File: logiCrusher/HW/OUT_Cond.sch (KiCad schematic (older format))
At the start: 21 parts

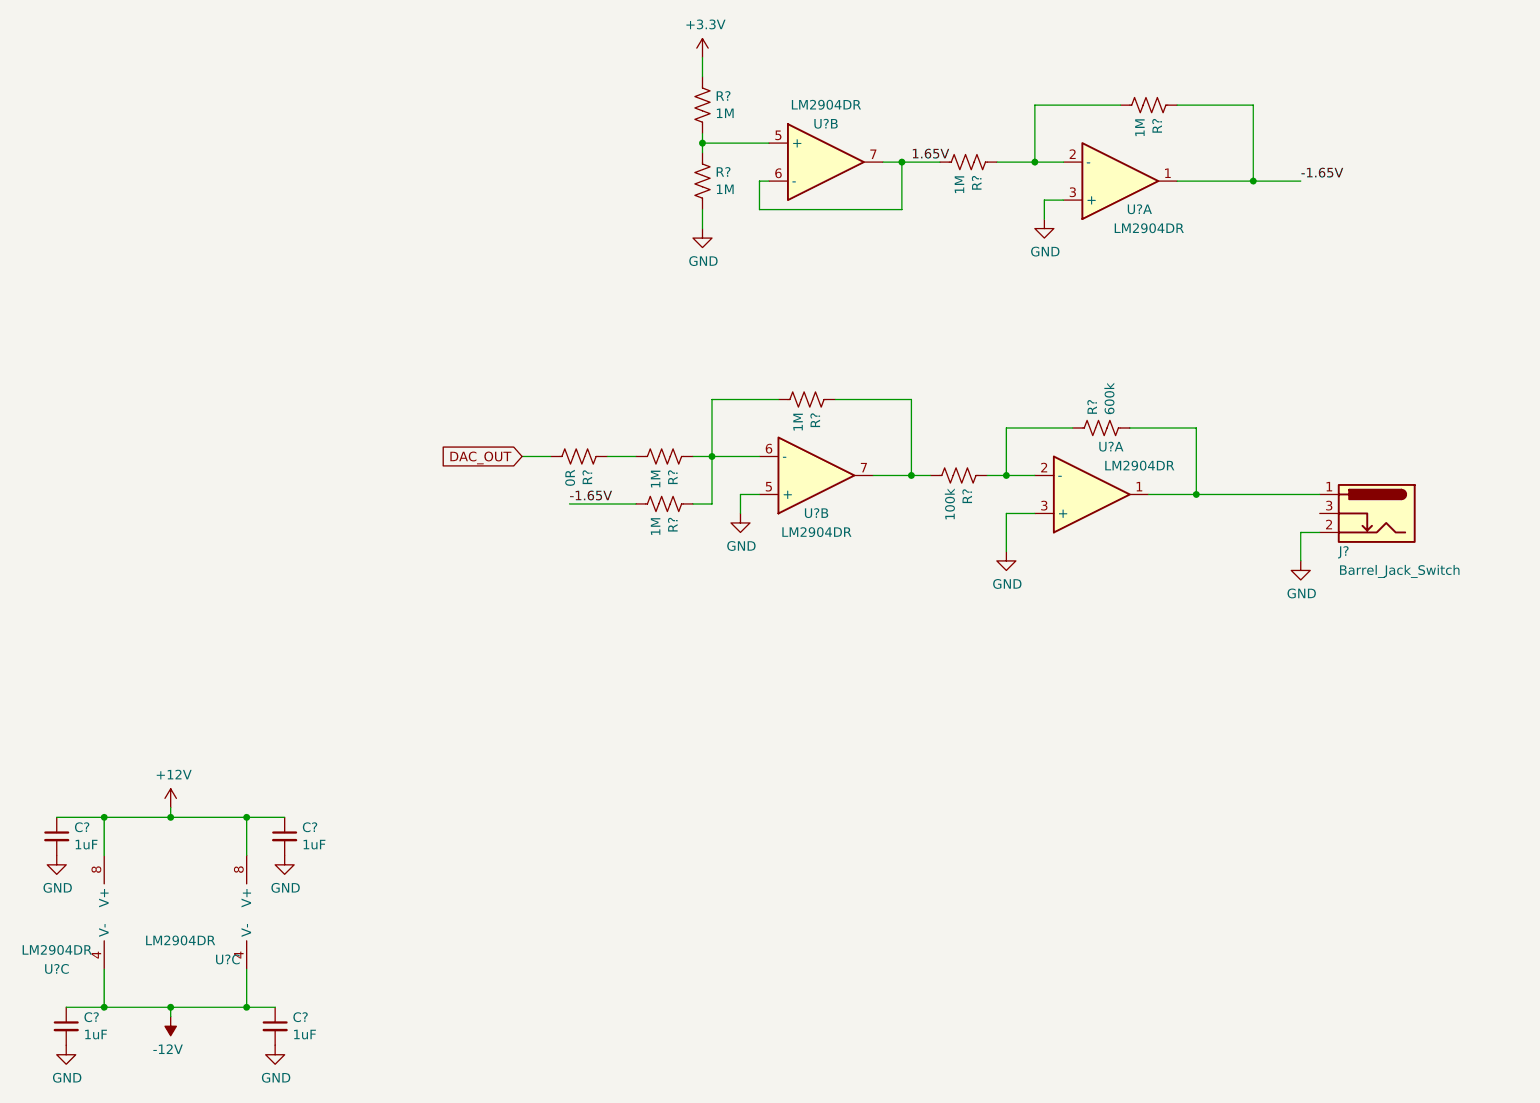
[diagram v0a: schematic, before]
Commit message: Added the front plate files
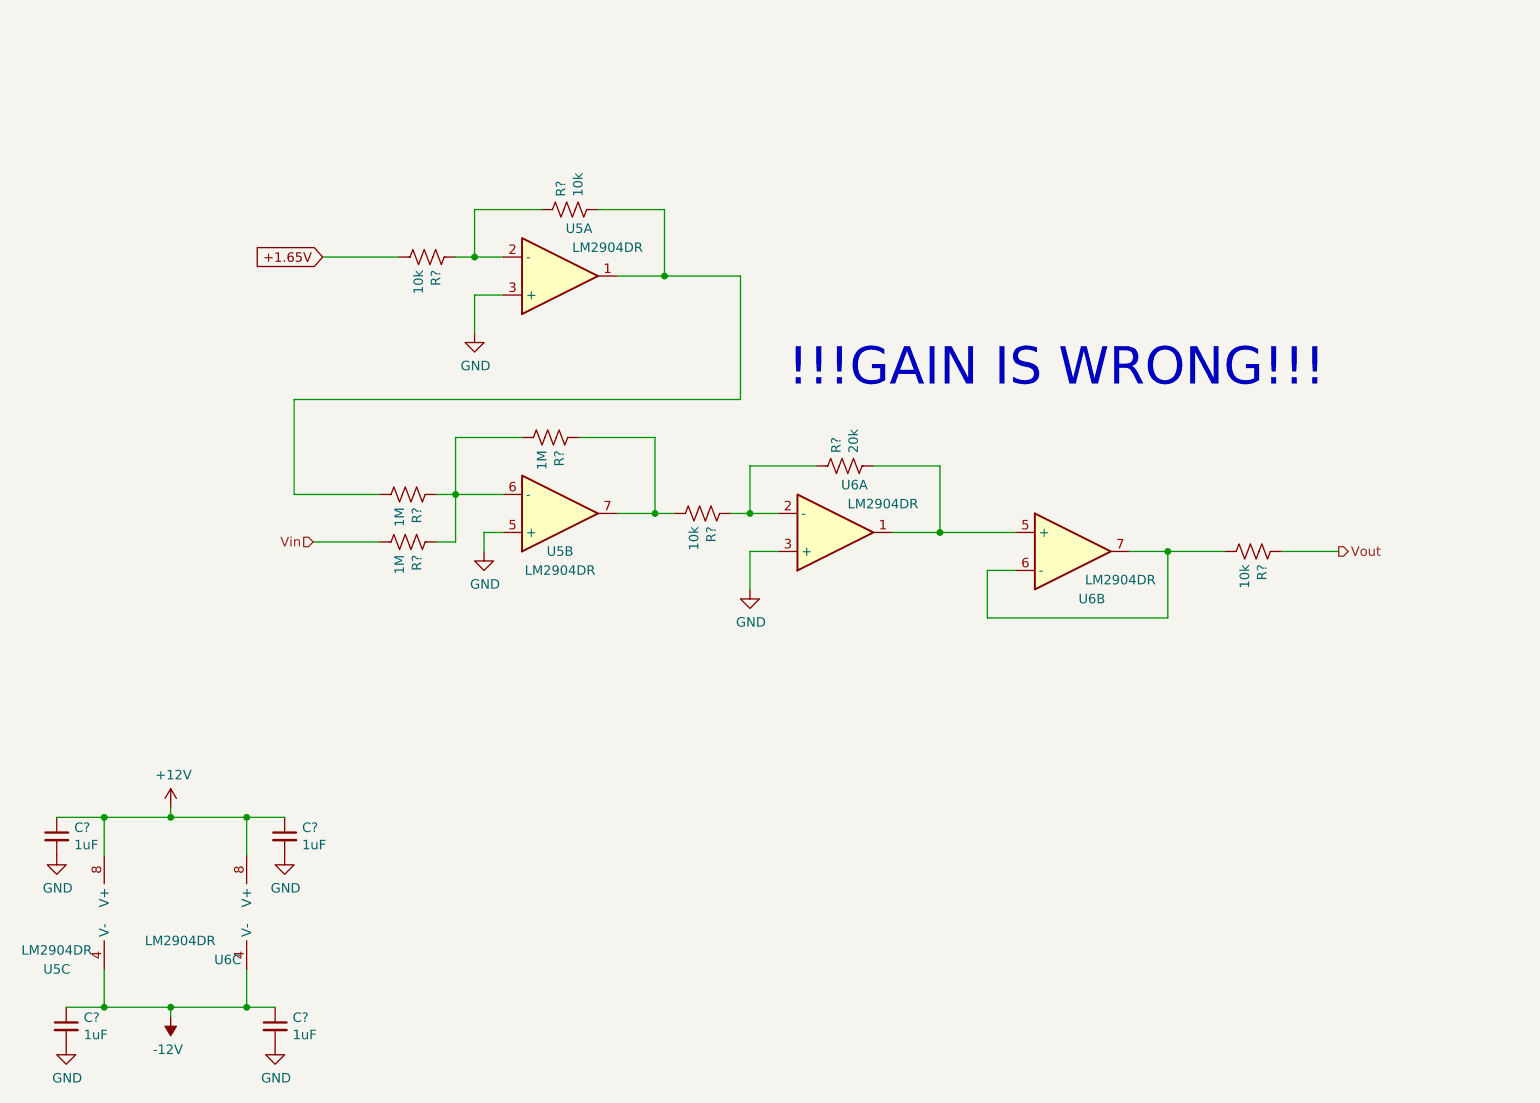
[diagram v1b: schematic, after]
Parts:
- removed J?: Barrel_Jack_Switch, Eurocad:PJ301M-12, symbol Connector:Barrel_Jack_Switch
- removed R?: 0R, Resistor_SMD:R_0805_2012Metric, symbol Device:R_US
- removed R? (x4): 1M, Resistor_SMD:R_0805_2012Metric, symbol Device:R_US
- removed U? (x2): LM2904DR, Package_SO:SOIC-8_3.9x4.9mm_P1.27mm, symbol Device:Opamp_Dual_Generic
- added R? (x3): 10k, Resistor_SMD:R_0805_2012Metric, symbol Device:R_US
- added unit 1 of U5
- added unit 2 of U6
- R?: value 600k -> 20k
- R?: value 100k -> 10k
- gave numbers to parts that had none: 2
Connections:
- net GND: now also U5.3 (+)
- net at R?.1: now also R?.1, U5.1
- net at R?.1, U6.1: now also U6.5 (+)
- net -1.65V renamed Vin
- new net: R?.1, U6.6 (-), U6.7
- new net: R?.2, R?.2, U5.2 (-)
- new net +1.65V: R?.1
- new net Vout: R?.2
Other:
- note added: "!!!GAIN IS WRONG!!!"
- moved on the sheet: R?, U5B, U6A

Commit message: Worked on the HW for the mcu module
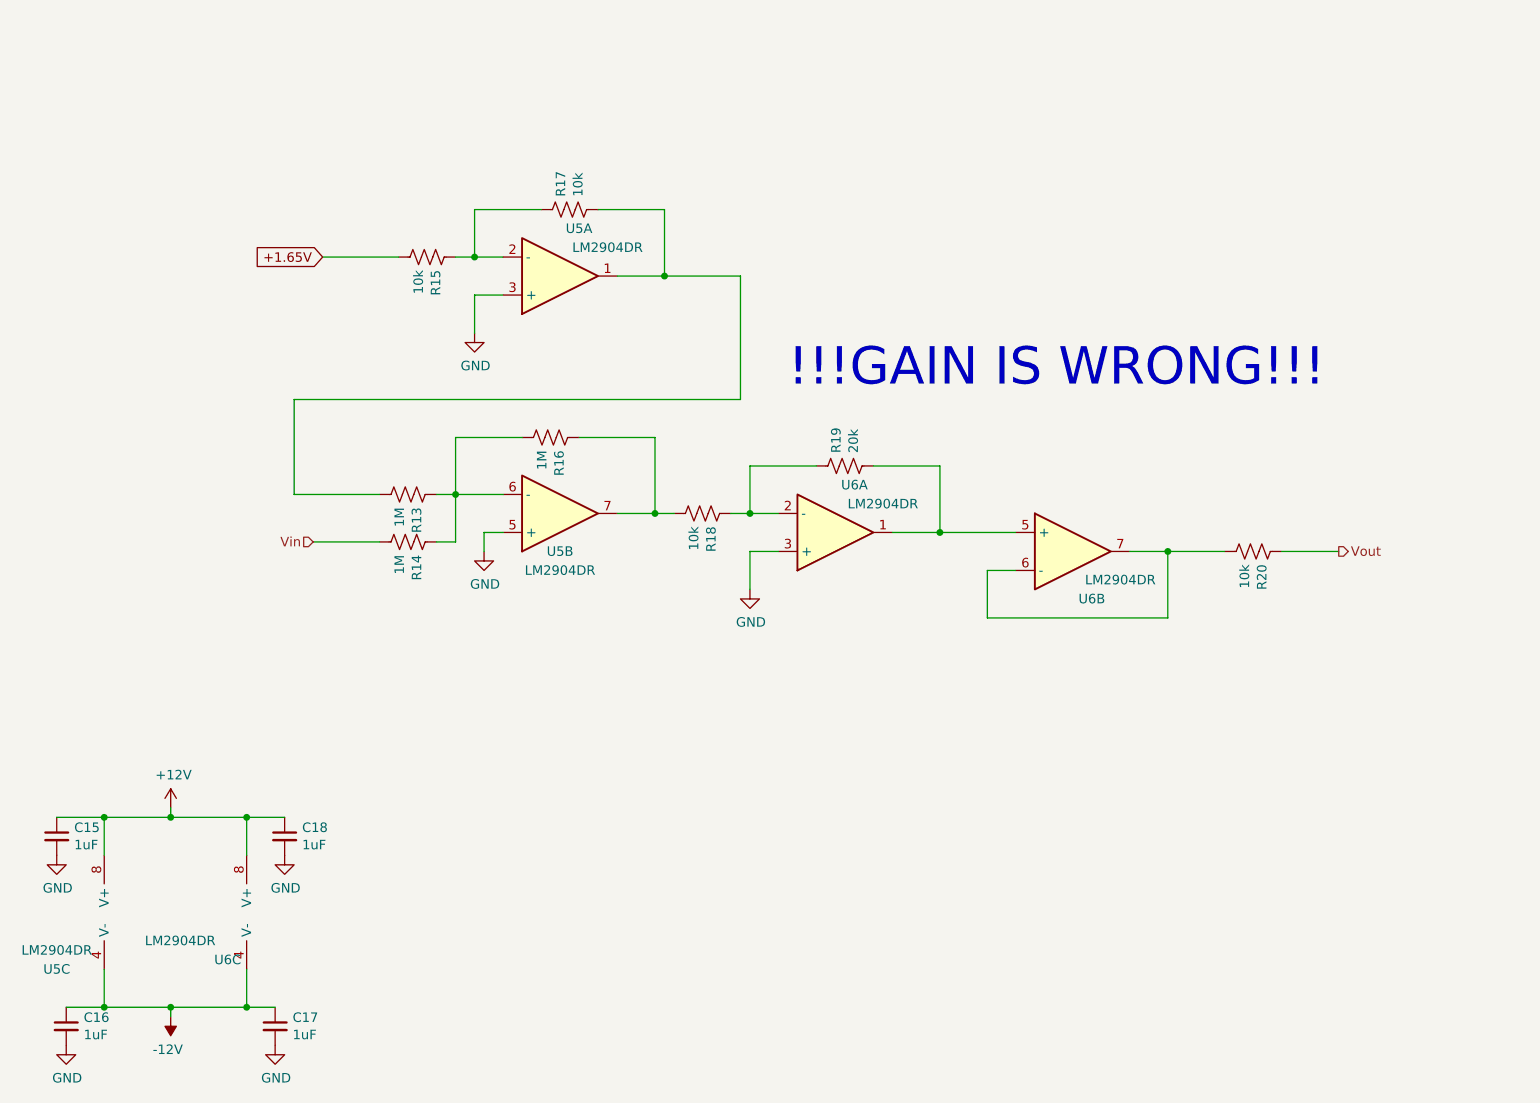
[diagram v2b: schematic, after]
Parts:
- gave numbers to parts that had none: 12
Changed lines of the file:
@@
 P 4750 4900
 AR Path="/5CBB18CB" Ref="#PWR?"  Part="1"
-AR Path="/5CBAEA8D/5CBB18CB" Ref="#PWR?"  Part="1"
-F 0 "#PWR?" H 4750 4650 50  0001 C CNN
+AR Path="/5CBAEA8D/5CBB18CB" Ref="#PWR053"  Part="1"
+F 0 "#PWR053" H 4750 4650 50  0001 C CNN
 F 1 "GND" H 4755 4727 50  0000 C CNN
 F 2 "" H 4750 4900 50  0001 C CNN
@@
 P 5250 4250
 AR Path="/5CBB18D3" Ref="R?"  Part="1"
-AR Path="/5CBAEA8D/5CBB18D3" Ref="R?"  Part="1"
-F 0 "R?" H 5182 4204 50  0000 R CNN
+AR Path="/5CBAEA8D/5CBB18D3" Ref="R19"  Part="1"
+F 0 "R19" H 5182 4204 50  0000 R CNN
 F 1 "20k" H 5182 4295 50  0000 R CNN
 F 2 "Resistor_SMD:R_0805_2012Metric" V 5290 4240 50  0001 C CNN
@@
 P 4500 4500
 AR Path="/5CBB18DA" Ref="R?"  Part="1"
-AR Path="/5CBAEA8D/5CBB18DA" Ref="R?"  Part="1"
-F 0 "R?" H 4432 4454 50  0000 R CNN
+AR Path="/5CBAEA8D/5CBB18DA" Ref="R18"  Part="1"
+F 0 "R18" H 4432 4454 50  0000 R CNN
 F 1 "10k" H 4432 4545 50  0000 R CNN
 F 2 "Resistor_SMD:R_0805_2012Metric" V 4540 4490 50  0001 C CNN
@@
 P 3700 4100
 AR Path="/5CBB18F1" Ref="R?"  Part="1"
-AR Path="/5CBAEA8D/5CBB18F1" Ref="R?"  Part="1"
-F 0 "R?" H 3632 4054 50  0000 R CNN
+AR Path="/5CBAEA8D/5CBB18F1" Ref="R16"  Part="1"
+F 0 "R16" H 3632 4054 50  0000 R CNN
 F 1 "1M" H 3632 4145 50  0000 R CNN
 F 2 "Resistor_SMD:R_0805_2012Metric" V 3740 4090 50  0001 C CNN
@@
 P 3350 4700
 AR Path="/5CBB1900" Ref="#PWR?"  Part="1"
-AR Path="/5CBAEA8D/5CBB1900" Ref="#PWR?"  Part="1"
-F 0 "#PWR?" H 3350 4450 50  0001 C CNN
+AR Path="/5CBAEA8D/5CBB1900" Ref="#PWR052"  Part="1"
+F 0 "#PWR052" H 3350 4450 50  0001 C CNN
 F 1 "GND" H 3355 4527 50  0000 C CNN
 F 2 "" H 3350 4700 50  0001 C CNN
@@
 P 2950 4650
 AR Path="/5CBB1908" Ref="R?"  Part="1"
-AR Path="/5CBAEA8D/5CBB1908" Ref="R?"  Part="1"
-F 0 "R?" H 2882 4604 50  0000 R CNN
+AR Path="/5CBAEA8D/5CBB1908" Ref="R14"  Part="1"
+F 0 "R14" H 2882 4604 50  0000 R CNN
 F 1 "1M" H 2882 4695 50  0000 R CNN
 F 2 "Resistor_SMD:R_0805_2012Metric" V 2990 4640 50  0001 C CNN
@@
 P 2950 4400
 AR Path="/5CBB190F" Ref="R?"  Part="1"
-AR Path="/5CBAEA8D/5CBB190F" Ref="R?"  Part="1"
-F 0 "R?" H 2882 4354 50  0000 R CNN
+AR Path="/5CBAEA8D/5CBB190F" Ref="R13"  Part="1"
+F 0 "R13" H 2882 4354 50  0000 R CNN
 F 1 "1M" H 2882 4445 50  0000 R CNN
 F 2 "Resistor_SMD:R_0805_2012Metric" V 2990 4390 50  0001 C CNN
@@
 $EndComp
 $Comp
-L power:+12V #PWR?
+L power:+12V #PWR047
 U 1 1 5CBB493F
 P 1700 6050
-F 0 "#PWR?" H 1700 5900 50  0001 C CNN
+F 0 "#PWR047" H 1700 5900 50  0001 C CNN
 F 1 "+12V" H 1715 6223 50  0000 C CNN
 F 2 "" H 1700 6050 50  0001 C CNN
@@
 $EndComp
 $Comp
-L power:-12V #PWR?
+L power:-12V #PWR048
 U 1 1 5CBB4945
 P 1700 7150
-F 0 "#PWR?" H 1700 7250 50  0001 C CNN
+F 0 "#PWR048" H 1700 7250 50  0001 C CNN
 F 1 "-12V" H 1715 7323 50  0000 C CNN
 F 2 "" H 1700 7150 50  0001 C CNN
@@
 	1700 7150 1700 7100
 $Comp
-L Device:C_Small C?
+L Device:C_Small C17
 U 1 1 5CBB4957
 P 2250 7200
-F 0 "C?" H 2342 7246 50  0000 L CNN
+F 0 "C17" H 2342 7246 50  0000 L CNN
 F 1 "1uF" H 2342 7155 50  0000 L CNN
 F 2 "Capacitor_SMD:C_0805_2012Metric" H 2250 7200 50  0001 C CNN
@@
 $EndComp
 $Comp
-L Device:C_Small C?
+L Device:C_Small C16
 U 1 1 5CBB495E
 P 1150 7200
-F 0 "C?" H 1242 7246 50  0000 L CNN
+F 0 "C16" H 1242 7246 50  0000 L CNN
 F 1 "1uF" H 1242 7155 50  0000 L CNN
 F 2 "Capacitor_SMD:C_0805_2012Metric" H 1150 7200 50  0001 C CNN
@@
 $EndComp
 $Comp
-L Device:C_Small C?
+L Device:C_Small C18
 U 1 1 5CBB4965
 P 2300 6200
-F 0 "C?" H 2392 6246 50  0000 L CNN
+F 0 "C18" H 2392 6246 50  0000 L CNN
 F 1 "1uF" H 2392 6155 50  0000 L CNN
 F 2 "Capacitor_SMD:C_0805_2012Metric" H 2300 6200 50  0001 C CNN
@@
 $EndComp
 $Comp
-L Device:C_Small C?
+L Device:C_Small C15
 U 1 1 5CBB496C
 P 1100 6200
-F 0 "C?" H 1192 6246 50  0000 L CNN
+F 0 "C15" H 1192 6246 50  0000 L CNN
 F 1 "1uF" H 1192 6155 50  0000 L CNN
 F 2 "Capacitor_SMD:C_0805_2012Metric" H 1100 6200 50  0001 C CNN
@@
 Connection ~ 1350 7100
 $Comp
-L power:GND #PWR?
+L power:GND #PWR045
 U 1 1 5CBB497B
 P 1100 6300
-F 0 "#PWR?" H 1100 6050 50  0001 C CNN
+F 0 "#PWR045" H 1100 6050 50  0001 C CNN
 F 1 "GND" H 1105 6127 50  0000 C CNN
 F 2 "" H 1100 6300 50  0001 C CNN
@@
 $EndComp
 $Comp
-L power:GND #PWR?
+L power:GND #PWR050
 U 1 1 5CBB4981
 P 2300 6300
-F 0 "#PWR?" H 2300 6050 50  0001 C CNN
+F 0 "#PWR050" H 2300 6050 50  0001 C CNN
 F 1 "GND" H 2305 6127 50  0000 C CNN
 F 2 "" H 2300 6300 50  0001 C CNN
@@
 $EndComp
 $Comp
-L power:GND #PWR?
+L power:GND #PWR049
 U 1 1 5CBB4987
 P 2250 7300
-F 0 "#PWR?" H 2250 7050 50  0001 C CNN
+F 0 "#PWR049" H 2250 7050 50  0001 C CNN
 F 1 "GND" H 2255 7127 50  0000 C CNN
 F 2 "" H 2250 7300 50  0001 C CNN
@@
 $EndComp
 $Comp
-L power:GND #PWR?
+L power:GND #PWR046
 U 1 1 5CBB498D
 P 1150 7300
-F 0 "#PWR?" H 1150 7050 50  0001 C CNN
+F 0 "#PWR046" H 1150 7050 50  0001 C CNN
 F 1 "GND" H 1155 7127 50  0000 C CNN
 F 2 "" H 1150 7300 50  0001 C CNN
@@
 P 7400 4700
 AR Path="/5CB6A68A" Ref="R?"  Part="1"
-AR Path="/5CBAEA8D/5CB6A68A" Ref="R?"  Part="1"
-F 0 "R?" H 7332 4654 50  0000 R CNN
+AR Path="/5CBAEA8D/5CB6A68A" Ref="R20"  Part="1"
+F 0 "R20" H 7332 4654 50  0000 R CNN
 F 1 "10k" H 7332 4745 50  0000 R CNN
 F 2 "Resistor_SMD:R_0805_2012Metric" V 7440 4690 50  0001 C CNN
@@
 P 3300 3550
 AR Path="/5CB6AC35" Ref="#PWR?"  Part="1"
-AR Path="/5CBAEA8D/5CB6AC35" Ref="#PWR?"  Part="1"
-F 0 "#PWR?" H 3300 3300 50  0001 C CNN
+AR Path="/5CBAEA8D/5CB6AC35" Ref="#PWR051"  Part="1"
+F 0 "#PWR051" H 3300 3300 50  0001 C CNN
 F 1 "GND" H 3305 3377 50  0000 C CNN
 F 2 "" H 3300 3550 50  0001 C CNN
@@
 P 3800 2900
 AR Path="/5CB6AC3D" Ref="R?"  Part="1"
-AR Path="/5CBAEA8D/5CB6AC3D" Ref="R?"  Part="1"
-F 0 "R?" H 3732 2854 50  0000 R CNN
+AR Path="/5CBAEA8D/5CB6AC3D" Ref="R17"  Part="1"
+F 0 "R17" H 3732 2854 50  0000 R CNN
 F 1 "10k" H 3732 2945 50  0000 R CNN
 F 2 "Resistor_SMD:R_0805_2012Metric" V 3840 2890 50  0001 C CNN
@@
 P 3050 3150
 AR Path="/5CB6AC44" Ref="R?"  Part="1"
-AR Path="/5CBAEA8D/5CB6AC44" Ref="R?"  Part="1"
-F 0 "R?" H 2982 3104 50  0000 R CNN
+AR Path="/5CBAEA8D/5CB6AC44" Ref="R15"  Part="1"
+F 0 "R15" H 2982 3104 50  0000 R CNN
 F 1 "10k" H 2982 3195 50  0000 R CNN
 F 2 "Resistor_SMD:R_0805_2012Metric" V 3090 3140 50  0001 C CNN

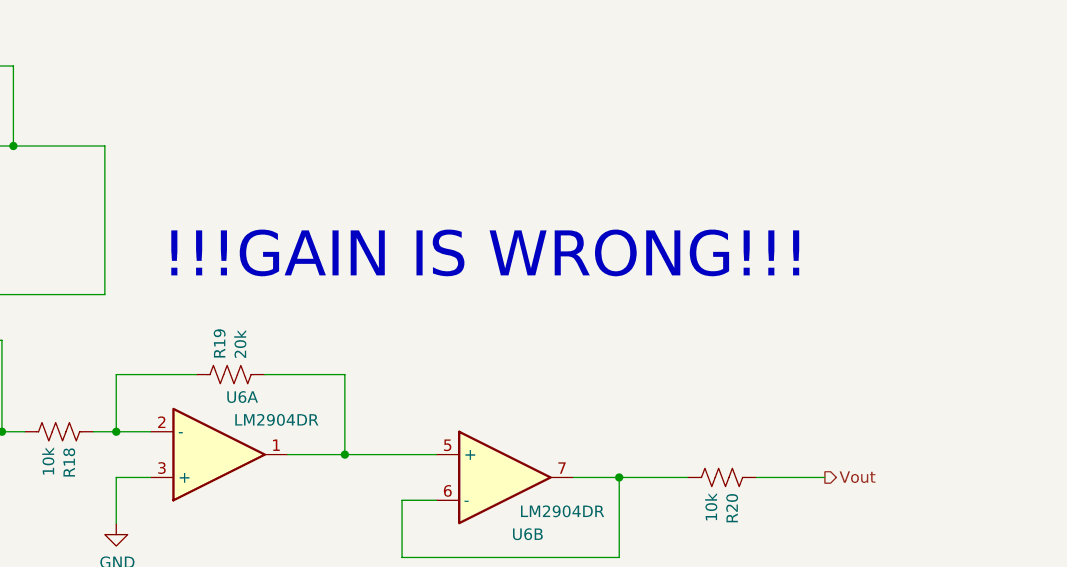
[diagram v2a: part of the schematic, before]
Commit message: Added simulation files and fixed the values of the gain resistors.
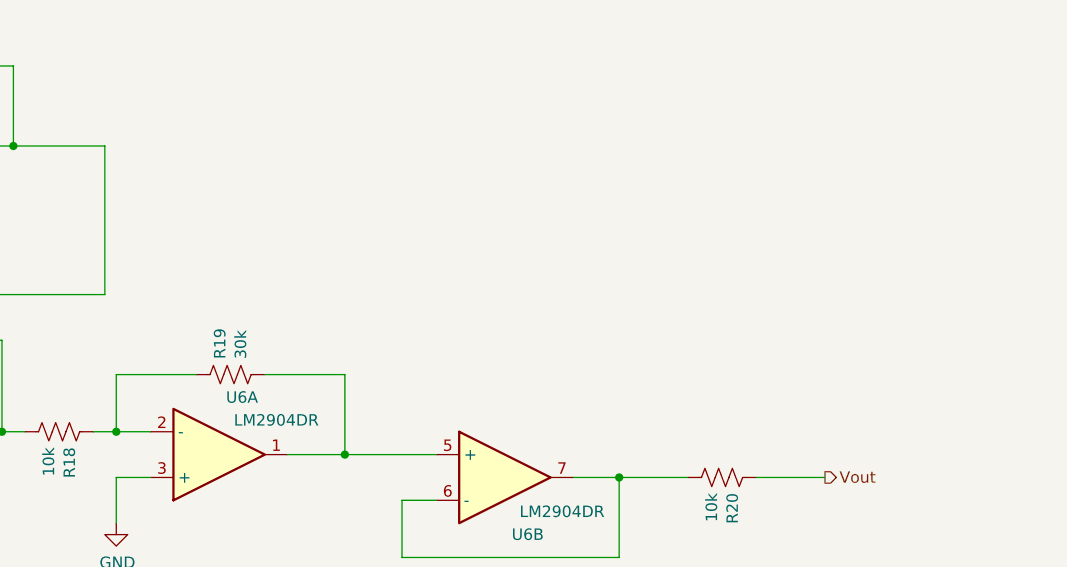
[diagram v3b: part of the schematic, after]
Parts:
- R19: value 20k -> 30k
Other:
- note removed: "!!!GAIN IS WRONG!!!"
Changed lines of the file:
@@
 AR Path="/5CBAEA8D/5CBB18D3" Ref="R19"  Part="1"
 F 0 "R19" H 5182 4204 50  0000 R CNN
-F 1 "20k" H 5182 4295 50  0000 R CNN
+F 1 "30k" H 5182 4295 50  0000 R CNN
 F 2 "Resistor_SMD:R_0805_2012Metric" V 5290 4240 50  0001 C CNN
 F 3 "~" H 5250 4250 50  0001 C CNN
@@
 Wire Wire Line
 	2350 4400 2800 4400
-Text Notes 4950 3850 0    197  ~ 0
-!!!GAIN IS WRONG!!!
 $EndSCHEMATC
